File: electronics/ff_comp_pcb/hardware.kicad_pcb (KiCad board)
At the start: 4 copper layers, 60 x 37 mm, 84 parts, among them J1 Micro_SD_Card_Det_Hirose_DM3AT, J2 USB_A, U1 AS4C512M16D3L-12BIN, U2 A33, U3 FSUSB42MUX, U4 RTL8188CUS, U5 RTL8188CUS, Y1 24Mhz, Y2 32.768khz

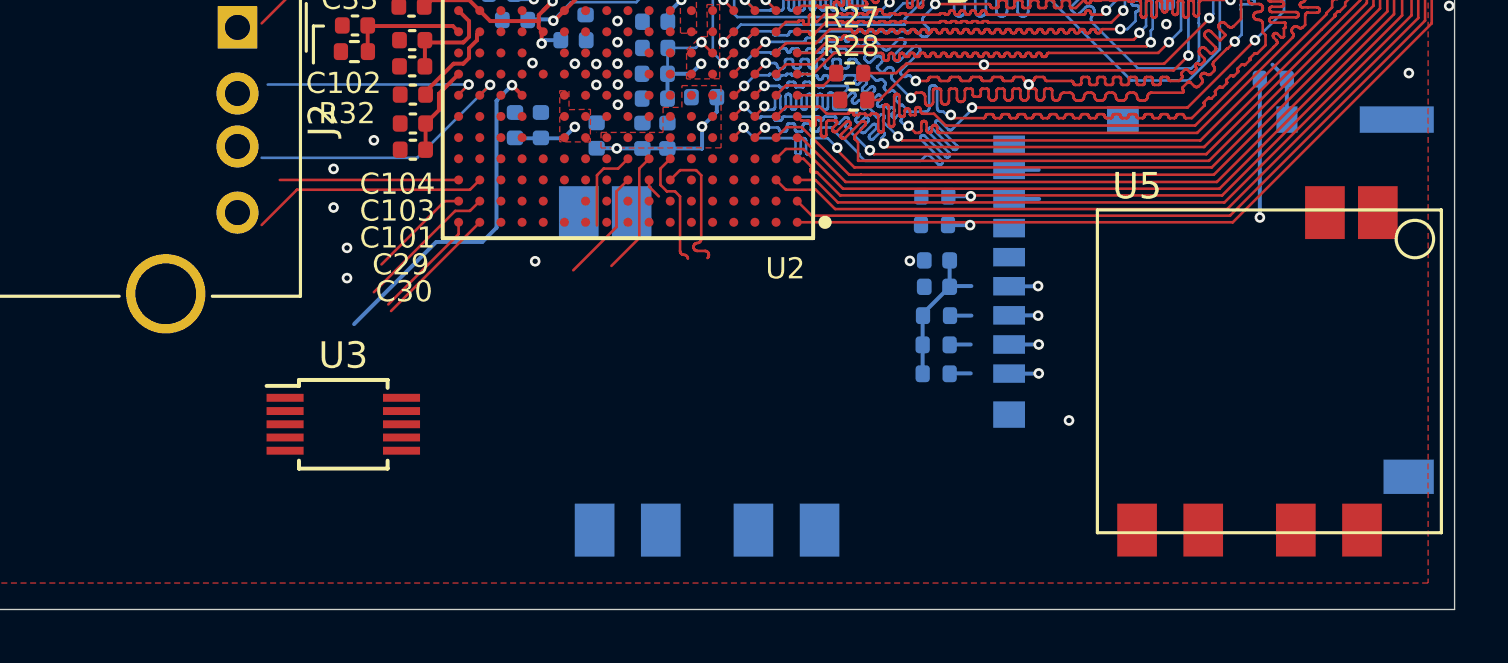
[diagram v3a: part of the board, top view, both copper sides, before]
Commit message: Added the step file of the board to the model, added a u.fl connector in.
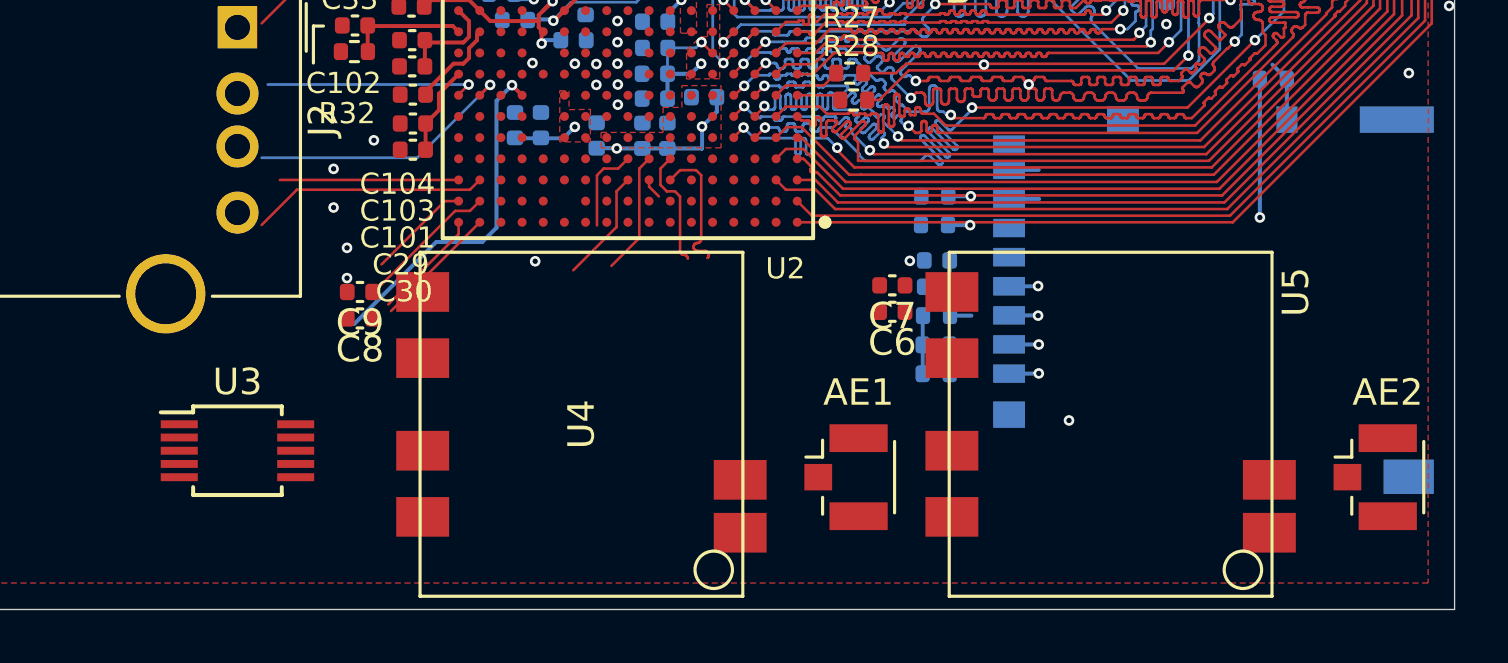
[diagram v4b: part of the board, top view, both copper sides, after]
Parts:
- added AE1: Antenna_Dipole, Connector_Coaxial:U.FL_Hirose_U.FL-R-SMT-1_Vertical, F.Cu at (123.0, 125.0)
- added AE2: Antenna_Dipole, Connector_Coaxial:U.FL_Hirose_U.FL-R-SMT-1_Vertical, F.Cu at (143.0, 125.0)
- added C6: 100nF, Capacitor_SMD:C_0402_1005Metric, F.Cu at (124.8, 118.8)
- added C7: 22uF, Capacitor_SMD:C_0402_1005Metric, F.Cu at (124.8, 117.8)
- added C8: 100nF, Capacitor_SMD:C_0402_1005Metric, F.Cu at (104.6, 119.0)
- added C9: 22uF, Capacitor_SMD:C_0402_1005Metric, F.Cu at (104.6, 118.0)
- U4: moved to F.Cu
- moved U5 6.32 mm to (133.0, 123.0), turned to 90 degrees
- moved U4 4.47 mm to (113.0, 123.0), turned to 90 degrees
- moved U3 4.12 mm to (100.0, 124.0)
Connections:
- J2 pad 1: Net-(J2-Pad1) -> (no net)
- J2 pad 2: Net-(J2-Pad2) -> (no net)
- J2 pad 3: Net-(J2-Pad3) -> (no net)
- J2 pad 4: Net-(J2-Pad4) -> (no net)
- U1 pad J1: Net-(U1-PadJ1) -> (no net)
- U1 pad J9: Net-(U1-PadJ9) -> (no net)
- U1 pad L1: Net-(U1-PadL1) -> (no net)
- U1 pad L9: Net-(U1-PadL9) -> (no net)
- U2 pad A10: Net-(U2-PadA10) -> (no net)
- U2 pad A11: Net-(U2-PadA11) -> (no net)
- U2 pad A12: Net-(U2-PadA12) -> (no net)
- U2 pad A13: Net-(U2-PadA13) -> (no net)
- U2 pad A14: Net-(U2-PadA14) -> (no net)
- U2 pad A15: Net-(U2-PadA15) -> (no net)
- U2 pad A16: /gpio/PG8 -> (no net)
- U2 pad A17: /gpio/PG6 -> (no net)
- U2 pad A2: Net-(U2-PadA2) -> (no net)
- U2 pad A3: Net-(U2-PadA3) -> (no net)
- U2 pad A4: Net-(U2-PadA4) -> (no net)
- U2 pad A5: Net-(U2-PadA5) -> (no net)
- U2 pad A6: Net-(U2-PadA6) -> (no net)
- U2 pad A7: Net-(U2-PadA7) -> (no net)
- U2 pad A8: Net-(U2-PadA8) -> (no net)
- U2 pad A9: Net-(U2-PadA9) -> (no net)
- U2 pad B10: Net-(U2-PadB10) -> (no net)
- U2 pad B11: Net-(U2-PadB11) -> (no net)
- U2 pad B13: Net-(U2-PadB13) -> (no net)
- U2 pad B14: Net-(U2-PadB14) -> (no net)
- U2 pad B15: Net-(U2-PadB15) -> (no net)
- U2 pad B16: /gpio/PG9 -> (no net)
- U2 pad B17: /gpio/PG7 -> (no net)
- U2 pad B2: Net-(U2-PadB2) -> (no net)
- U2 pad B3: Net-(U2-PadB3) -> (no net)
- U2 pad B4: Net-(U2-PadB4) -> (no net)
- U2 pad B5: Net-(U2-PadB5) -> (no net)
- U2 pad B6: Net-(U2-PadB6) -> (no net)
- U2 pad B7: Net-(U2-PadB7) -> (no net)
- U2 pad B8: Net-(U2-PadB8) -> (no net)
- U2 pad B9: Net-(U2-PadB9) -> (no net)
- U2 pad C10: Net-(U2-PadC10) -> (no net)
- U2 pad C11: Net-(U2-PadC11) -> (no net)
- U2 pad C12: Net-(U2-PadC12) -> (no net)
- U2 pad C13: Net-(U2-PadC13) -> (no net)
- U2 pad C14: Net-(U2-PadC14) -> (no net)
- U2 pad C15: Net-(U2-PadC15) -> (no net)
- U2 pad C16: /gpio/PG11 -> (no net)
- U2 pad C17: /gpio/PG10 -> (no net)
- U2 pad C3: Net-(U2-PadC3) -> (no net)
- U2 pad C4: Net-(U2-PadC4) -> (no net)
- U2 pad C5: Net-(U2-PadC5) -> (no net)
- U2 pad C6: Net-(U2-PadC6) -> (no net)
- U2 pad D10: Net-(U2-PadD10) -> (no net)
- U2 pad D11: Net-(U2-PadD11) -> (no net)
- U2 pad D12: Net-(U2-PadD12) -> (no net)
- U2 pad D13: Net-(U2-PadD13) -> (no net)
- U2 pad D14: Net-(U2-PadD14) -> (no net)
- U2 pad D15: Net-(U2-PadD15) -> (no net)
- U2 pad D16: Net-(U2-PadD16) -> (no net)
- U2 pad D17: Net-(U2-PadD17) -> (no net)
- U2 pad D3: Net-(U2-PadD3) -> (no net)
- U2 pad D4: Net-(U2-PadD4) -> (no net)
- U2 pad D5: Net-(U2-PadD5) -> (no net)
- U2 pad D6: Net-(U2-PadD6) -> (no net)
- U2 pad E14: Net-(U2-PadE14) -> (no net)
- U2 pad E15: Net-(U2-PadE15) -> (no net)
- U2 pad E16: Net-(U2-PadE16) -> (no net)
- U2 pad E17: Net-(U2-PadE17) -> (no net)
- U2 pad F14: Net-(U2-PadF14) -> (no net)
- U2 pad F15: Net-(U2-PadF15) -> (no net)
- U2 pad F16: Net-(U2-PadF16) -> (no net)
- U2 pad F17: Net-(U2-PadF17) -> (no net)
- U2 pad G15: Net-(U2-PadG15) -> (no net)
- U2 pad G16: /gpio/UART0_RX -> (no net)
- U2 pad G17: /gpio/UART0_TX -> (no net)
- U2 pad H14: Net-(U2-PadH14) -> (no net)
- U2 pad H15: Net-(U2-PadH15) -> (no net)
- U2 pad H16: Net-(U2-PadH16) -> (no net)
- U2 pad J14: Net-(U2-PadJ14) -> (no net)
- U2 pad J15: Net-(U2-PadJ15) -> (no net)
- U2 pad J16: Net-(U2-PadJ16) -> (no net)
- U2 pad J17: Net-(U2-PadJ17) -> (no net)
- U2 pad K14: Net-(U2-PadK14) -> (no net)
- U2 pad K15: Net-(U2-PadK15) -> (no net)
- U2 pad L14: Net-(U2-PadL14) -> (no net)
- U2 pad L15: Net-(U2-PadL15) -> (no net)
- U2 pad L7: Net-(U2-PadL7) -> (no net)
- U2 pad M15: Net-(U2-PadM15) -> (no net)
- U2 pad M16: Net-(U2-PadM16) -> (no net)
- U2 pad M17: Net-(U2-PadM17) -> (no net)
- U2 pad N15: Net-(U2-PadN15) -> (no net)
- U2 pad N16: Net-(U2-PadN16) -> (no net)
- U2 pad N17: Net-(U2-PadN17) -> (no net)
- U2 pad N5: Net-(U2-PadN5) -> (no net)
- U2 pad N7: Net-(U2-PadN7) -> (no net)
- U2 pad P10: Net-(U2-PadP10) -> (no net)
- U2 pad P11: Net-(U2-PadP11) -> (no net)
- U2 pad P12: Net-(U2-PadP12) -> (no net)
- U2 pad P13: Net-(U2-PadP13) -> (no net)
- U2 pad P14: Net-(U2-PadP14) -> (no net)
- U2 pad P15: Net-(U2-PadP15) -> (no net)
- U2 pad P16: Net-(U2-PadP16) -> (no net)
- U2 pad P4: Net-(U2-PadP4) -> (no net)
- U2 pad P5: Net-(U2-PadP5) -> (no net)
- U2 pad P6: Net-(U2-PadP6) -> (no net)
- U2 pad P7: Net-(U2-PadP7) -> (no net)
- U2 pad P8: Net-(U2-PadP8) -> (no net)
- U2 pad P9: Net-(U2-PadP9) -> (no net)
- U2 pad R10: Net-(U2-PadR10) -> (no net)
- U2 pad R11: Net-(U2-PadR11) -> (no net)
- U2 pad R12: Net-(U2-PadR12) -> (no net)
- U2 pad R13: Net-(U2-PadR13) -> (no net)
- U2 pad R14: Net-(U2-PadR14) -> (no net)
- U2 pad R15: Net-(U2-PadR15) -> (no net)
- U2 pad R4: Net-(U2-PadR4) -> (no net)
- U2 pad R5: Net-(U2-PadR5) -> (no net)
- U2 pad R6: Net-(U2-PadR6) -> (no net)
- U2 pad R7: Net-(U2-PadR7) -> (no net)
- U2 pad R8: Net-(U2-PadR8) -> (no net)
- U2 pad R9: Net-(U2-PadR9) -> (no net)
- U2 pad T10: Net-(U2-PadT10) -> (no net)
- U2 pad T11: Net-(U2-PadT11) -> (no net)
- U2 pad T12: Net-(U2-PadT12) -> (no net)
- U2 pad T13: Net-(U2-PadT13) -> (no net)
- U2 pad T14: Net-(U2-PadT14) -> (no net)
- U2 pad T15: Net-(U2-PadT15) -> (no net)
- U2 pad T16: Net-(U2-PadT16) -> (no net)
- U2 pad T17: Net-(U2-PadT17) -> (no net)
- U2 pad T5: Net-(U2-PadT5) -> (no net)
- U2 pad T6: Net-(U2-PadT6) -> (no net)
- U2 pad T7: Net-(U2-PadT7) -> (no net)
- U2 pad T8: Net-(U2-PadT8) -> (no net)
- U2 pad T9: Net-(U2-PadT9) -> (no net)
- U2 pad U10: Net-(U2-PadU10) -> (no net)
- U2 pad U11: Net-(U2-PadU11) -> (no net)
- U2 pad U12: Net-(U2-PadU12) -> (no net)
- U2 pad U13: Net-(U2-PadU13) -> (no net)
- U2 pad U14: Net-(U2-PadU14) -> (no net)
- U2 pad U15: Net-(U2-PadU15) -> (no net)
- U2 pad U16: Net-(U2-PadU16) -> (no net)
- U2 pad U17: Net-(U2-PadU17) -> (no net)
- U2 pad U5: Net-(U2-PadU5) -> (no net)
- U2 pad U6: Net-(U2-PadU6) -> (no net)
- U2 pad U7: Net-(U2-PadU7) -> (no net)
- U2 pad U8: Net-(U2-PadU8) -> (no net)
- U2 pad U9: Net-(U2-PadU9) -> (no net)
- U3 pad 1: Net-(U3-Pad1) -> (no net)
- U3 pad 10: Net-(U3-Pad10) -> (no net)
- U3 pad 2: Net-(U3-Pad2) -> (no net)
- U3 pad 3: Net-(U3-Pad3) -> (no net)
- U3 pad 4: Net-(U3-Pad4) -> (no net)
- U3 pad 5: Net-(U3-Pad5) -> (no net)
- U3 pad 6: Net-(U3-Pad6) -> (no net)
- U3 pad 7: Net-(U3-Pad7) -> (no net)
- U3 pad 8: Net-(U3-Pad8) -> (no net)
- U3 pad 9: Net-(U3-Pad9) -> (no net)
- U4 pad 1: Net-(U4-Pad1) -> GND
- U4 pad 2: Net-(U4-Pad2) -> /gpio/RF1
- U4 pad 3: Net-(U4-Pad3) -> +3V3
- U4 pad 4: Net-(U4-Pad4) -> (no net)
- U4 pad 5: Net-(U4-Pad5) -> (no net)
- U4 pad 6: Net-(U4-Pad6) -> GND
- U5 pad 1: Net-(U5-Pad1) -> GND
- U5 pad 2: Net-(U5-Pad2) -> /gpio/RF2
- U5 pad 3: Net-(U5-Pad3) -> +3V3
- U5 pad 4: Net-(U5-Pad4) -> (no net)
- U5 pad 5: Net-(U5-Pad5) -> (no net)
- U5 pad 6: Net-(U5-Pad6) -> GND
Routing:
- net (no net): track 0.00 -> 56.0 mm, vias 0 -> 4
- net /gpio/UART0_RX: track 10.3 -> 0.00 mm, vias 1 -> 0
- net /gpio/PG11: track 8.95 -> 0.00 mm
- net /gpio/UART0_TX: track 8.16 -> 0.00 mm, vias 1 -> 0
- net /gpio/PG10: track 6.76 -> 0.00 mm
- net /gpio/PG9: track 5.43 -> 0.00 mm
- net /gpio/PG8: track 4.74 -> 0.00 mm
- net /gpio/PG6: track 4.20 -> 0.00 mm
- net /gpio/PG7: track 3.90 -> 0.00 mm
- net Net-(U2-PadT17): track 1.74 -> 0.00 mm, vias 1 -> 0
- net Net-(U2-PadU16): track 0.62 -> 0.00 mm
- net Net-(U2-PadU17): track 0.56 -> 0.00 mm
- net Net-(U2-PadT16): track 0.56 -> 0.00 mm, vias 1 -> 0

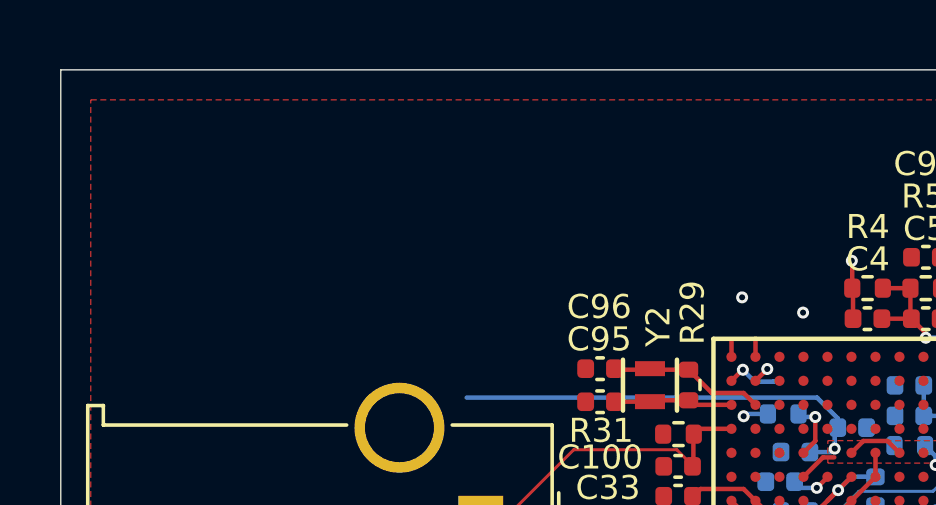
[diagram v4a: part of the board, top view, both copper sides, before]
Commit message: Dropped down the board to board.
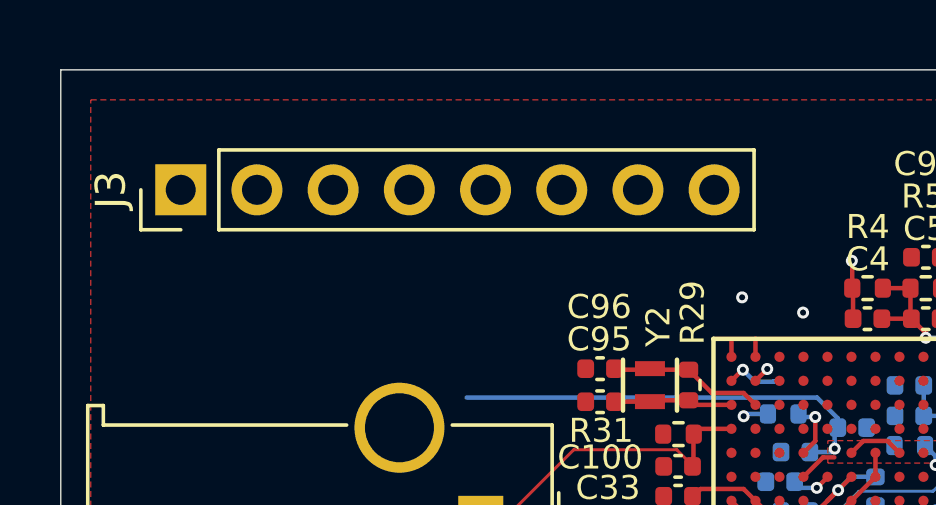
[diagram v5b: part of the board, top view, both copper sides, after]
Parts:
- added J3: Conn_01x08_Female, Connector_PinHeader_2.54mm:PinHeader_1x08_P2.54mm_Vertical, F.Cu at (90.0, 97.0)
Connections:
- J2 pad 1: (no net) -> +5V
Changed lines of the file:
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@@
     (tracks 17952)
     (zones 0)
-    (modules 90)
-    (nets 85)
+    (modules 91)
+    (nets 86)
   )
   (page A4)
@@
   (net 83 /gpio/RF1)
   (net 84 /gpio/RF2)
+  (net 85 +5V)
   (net_class Default "This is the default net class."
     (clearance 0.15)
@@
     (add_net +3V0)
     (add_net +3V3)
+    (add_net +5V)
     (add_net /DVREF)
     (add_net /HPVCCBP)
     (add_net /VCC-EFUSE)
+    (add_net /gpio/PG9)
     (add_net /gpio/RESET)
     (add_net /gpio/RF1)
@@
     (add_net "Net-(C98-Pad1)")
     (add_net "Net-(C99-Pad1)")
-    (add_net "Net-(J2-Pad1)")
     (add_net "Net-(J2-Pad2)")
     (add_net "Net-(J2-Pad3)")
@@
     (uvia_drill 0.6)
   )
+  (module Connector_PinHeader_2.54mm:PinHeader_1x08_P2.54mm_Vertical (layer F.Cu)
+    (at 90 97 90)
+    (descr "Through hole straight pin header, 1x08, 2.54mm pitch, single row")
+    (tags "Through hole pin header THT 1x08 2.54mm single row")
+    (fp_text reference J3 (at 0 -2.33 90) (layer F.SilkS)
+      (effects (font (size 1 1) (thickness 0.15)))
+    )
+    (fp_text value Conn_01x08_Female (at 0 20.11 90) (layer F.Fab)
+      (effects (font (size 1 1) (thickness 0.15)))
+    )
+    (fp_text user %R (at 0 8.89) (layer F.Fab)
+      (effects (font (size 1 1) (thickness 0.15)))
+    )
+    (fp_line (start -0.635 -1.27) (end 1.27 -1.27) (layer F.Fab) (width 0.1))
+    (fp_line (start 1.27 -1.27) (end 1.27 19.05) (layer F.Fab) (width 0.1))
+    (fp_line (start 1.27 19.05) (end -1.27 19.05) (layer F.Fab) (width 0.1))
+    (fp_line (start -1.27 19.05) (end -1.27 -0.635) (layer F.Fab) (width 0.1))
+    (fp_line (start -1.27 -0.635) (end -0.635 -1.27) (layer F.Fab) (width 0.1))
+    (fp_line (start -1.33 19.11) (end 1.33 19.11) (layer F.SilkS) (width 0.12))
+    (fp_line (start -1.33 1.27) (end -1.33 19.11) (layer F.SilkS) (width 0.12))
+    (fp_line (start 1.33 1.27) (end 1.33 19.11) (layer F.SilkS) (width 0.12))
+    (fp_line (start -1.33 1.27) (end 1.33 1.27) (layer F.SilkS) (width 0.12))
+    (fp_line (start -1.33 0) (end -1.33 -1.33) (layer F.SilkS) (width 0.12))
+    (fp_line (start -1.33 -1.33) (end 0 -1.33) (layer F.SilkS) (width 0.12))
+    (fp_line (start -1.8 -1.8) (end -1.8 19.55) (layer F.CrtYd) (width 0.05))
+    (fp_line (start -1.8 19.55) (end 1.8 19.55) (layer F.CrtYd) (width 0.05))
+    (fp_line (start 1.8 19.55) (end 1.8 -1.8) (layer F.CrtYd) (width 0.05))
+    (fp_line (start 1.8 -1.8) (end -1.8 -1.8) (layer F.CrtYd) (width 0.05))
+    (pad 8 thru_hole oval (at 0 17.78 90) (size 1.7 1.7) (drill 1) (layers *.Cu *.Mask)
+      (net 34 GND))
+    (pad 7 thru_hole oval (at 0 15.24 90) (size 1.7 1.7) (drill 1) (layers *.Cu *.Mask)
+      (net 58 +1V1))
+    (pad 6 thru_hole oval (at 0 12.7 90) (size 1.7 1.7) (drill 1) (layers *.Cu *.Mask)
+      (net 33 +1V35))
+    (pad 5 thru_hole oval (at 0 10.16 90) (size 1.7 1.7) (drill 1) (layers *.Cu *.Mask)
+      (net 57 +2V5))
+    (pad 4 thru_hole oval (at 0 7.62 90) (size 1.7 1.7) (drill 1) (layers *.Cu *.Mask)
+      (net 59 +3V0))
+    (pad 3 thru_hole oval (at 0 5.08 90) (size 1.7 1.7) (drill 1) (layers *.Cu *.Mask)
+      (net 60 +3V3))
+    (pad 2 thru_hole oval (at 0 2.54 90) (size 1.7 1.7) (drill 1) (layers *.Cu *.Mask)
+      (net 85 +5V))
+    (pad 1 thru_hole rect (at 0 0 90) (size 1.7 1.7) (drill 1) (layers *.Cu *.Mask)
+      (net 34 GND))
+    (model ${KISYS3DMOD}/Connector_PinHeader_2.54mm.3dshapes/PinHeader_1x08_P2.54mm_Vertical.wrl
+      (at (xyz 0 0 0))
+      (scale (xyz 1 1 1))
+      (rotate (xyz 0 0 0))
+    )
+  )
   (module Connector_Coaxial:U.FL_Hirose_U.FL-R-SMT-1_Vertical (layer F.Cu)
     (at 143 125)
@@
     (pad 3 thru_hole circle (at 4.5 0 270) (size 1.6 1.6) (drill 0.95) (layers *.Cu *.Mask))
     (pad 2 thru_hole circle (at 2.5 0 270) (size 1.6 1.6) (drill 0.95) (layers *.Cu *.Mask))
-    (pad 1 thru_hole rect (at 0 0 270) (size 1.6 1.5) (drill 0.95) (layers *.Cu *.Mask))
+    (pad 1 thru_hole rect (at 0 0 270) (size 1.6 1.5) (drill 0.95) (layers *.Cu *.Mask)
+      (net 85 +5V))
     (pad 5 thru_hole circle (at 10.07 2.71 270) (size 3 3) (drill 2.3) (layers *.Cu *.Mask)
       (net 82 "Net-(J2-Pad5)"))

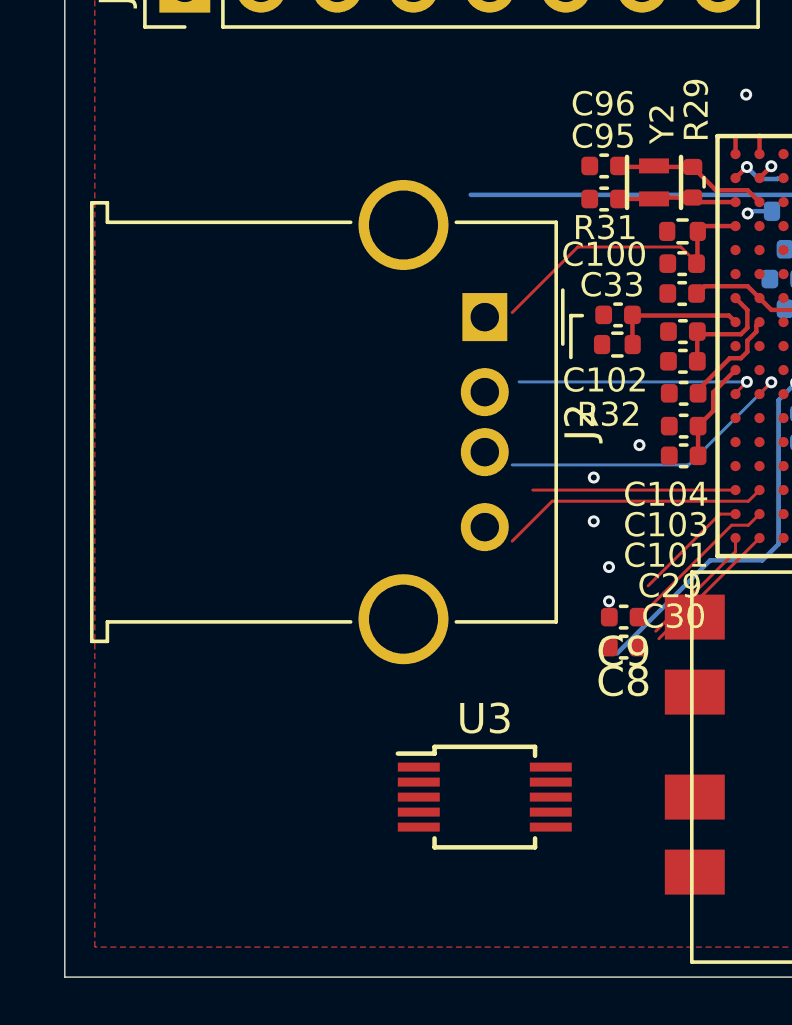
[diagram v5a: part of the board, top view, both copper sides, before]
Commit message: Put a mounting hole in the board.
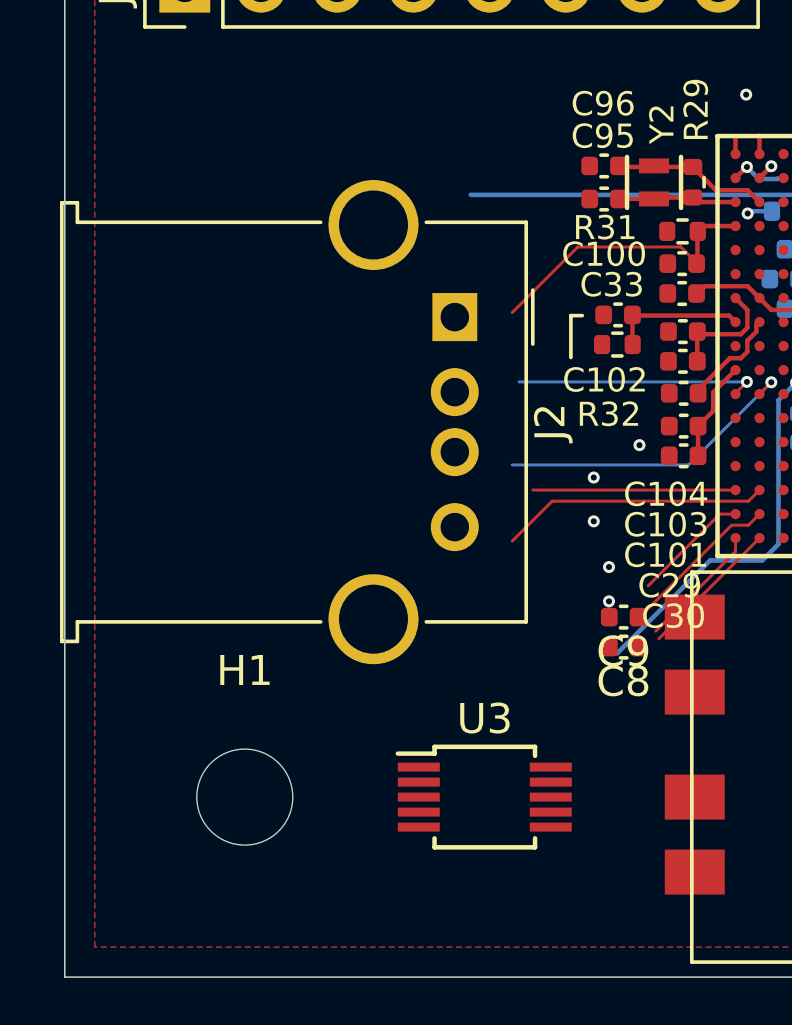
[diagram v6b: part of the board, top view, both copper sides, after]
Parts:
- added H1: MountingHole, MountingHole:MountingHole_3.2mm_M3, F.Cu at (92.0, 124.0)
- moved J2 1.00 mm to (99.0, 108.0)
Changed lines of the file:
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@@
     (tracks 17952)
     (zones 0)
-    (modules 91)
+    (modules 92)
     (nets 86)
   )
@@
     (uvia_drill 0.6)
   )
+  (module MountingHole:MountingHole_3.2mm_M3 (layer F.Cu)
+    (at 92 124)
+    (descr "Mounting Hole 3.2mm, no annular, M3")
+    (tags "mounting hole 3.2mm no annular m3")
+    (attr virtual)
+    (fp_text reference H1 (at 0 -4.2) (layer F.SilkS)
+      (effects (font (size 1 1) (thickness 0.15)))
+    )
+    (fp_text value MountingHole (at 0 4.2) (layer F.Fab)
+      (effects (font (size 1 1) (thickness 0.15)))
+    )
+    (fp_text user %R (at 0.3 0) (layer F.Fab)
+      (effects (font (size 1 1) (thickness 0.15)))
+    )
+    (fp_circle (center 0 0) (end 3.2 0) (layer Cmts.User) (width 0.15))
+    (fp_circle (center 0 0) (end 3.45 0) (layer F.CrtYd) (width 0.05))
+    (pad 1 np_thru_hole circle (at 0 0) (size 3.2 3.2) (drill 3.2) (layers *.Cu *.Mask))
+  )
   (module Connector_PinHeader_2.54mm:PinHeader_1x08_P2.54mm_Vertical (layer F.Cu)
     (at 90 97 90)
@@
   )
   (module Connector_USB:USB_A_Molex_67643_Horizontal (layer F.Cu)
-    (at 100 108 270)
+    (at 99 108 270)
     (descr "USB type A, Horizontal, https://www.molex.com/pdm_docs/sd/676433910_sd.pdf")
     (tags "USB_A Female Connector receptacle")
